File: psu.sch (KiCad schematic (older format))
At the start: 15 parts

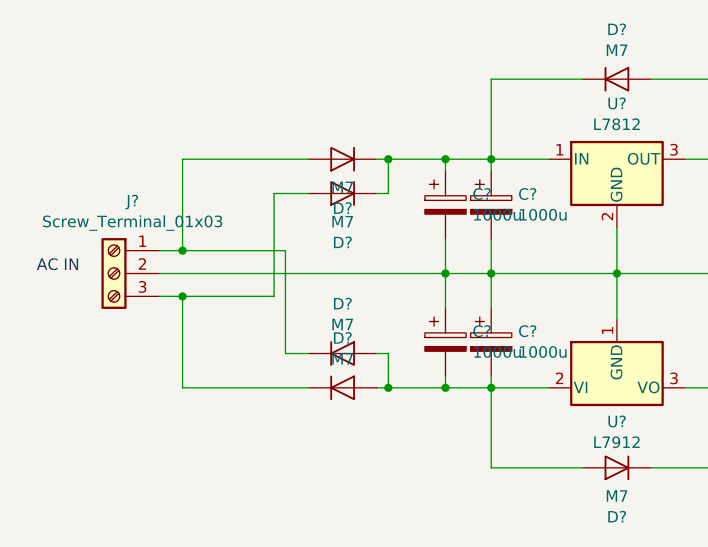
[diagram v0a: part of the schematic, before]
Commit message: adjusted some caps in PSU and rumble filter
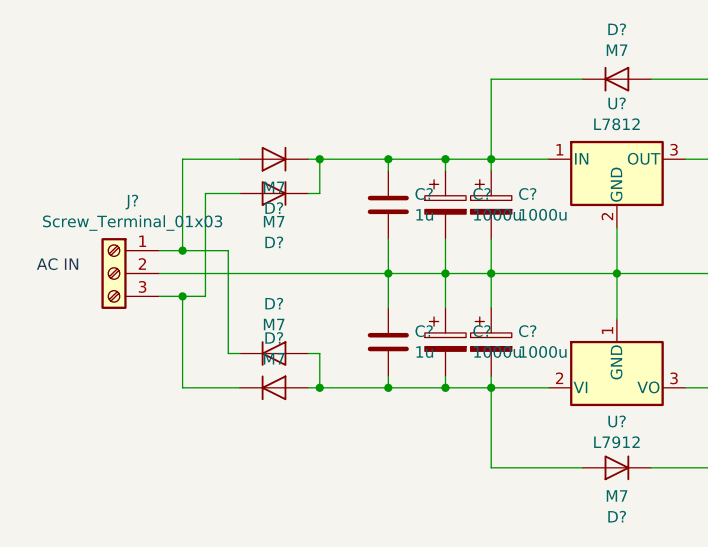
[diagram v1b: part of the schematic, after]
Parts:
- added C? (x2): 1u, Capacitors_SMD:C_0805, symbol Device:C
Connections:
- net GND: now also C?.1, C?.2
- net at C?.1, C?.1, D?.1 (K)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: now also C?.1
- net at C?.2, C?.2, D?.2 (A)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: now also C?.2
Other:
- moved on the sheet: D?
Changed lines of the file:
@@
 	3850 2200 3850 2350
-Wire Wire Line
-	3550 1700 3600 1700
 Wire Wire Line
 	3850 1700 3850 1750
@@
 	4050 1700 4300 1700
 Wire Wire Line
-	3550 2700 3600 2700
+	3250 2700 3300 2700
 Wire Wire Line
 	4050 2650 4050 2700
@@
 L Device:D D?
 U 1 1 61A5C1E5
-P 3400 1700
-F 0 "D?" H 3400 1916 50  0000 C CNN
-F 1 "M7" H 3400 1825 50  0000 C CNN
-F 2 "Diodes_SMD:D_SMA" H 3400 1700 50  0001 C CNN
-F 3 "~" H 3400 1700 50  0001 C CNN
-	1    3400 1700
+P 3100 1700
+F 0 "D?" H 3100 1916 50  0000 C CNN
+F 1 "M7" H 3100 1825 50  0000 C CNN
+F 2 "Diodes_SMD:D_SMA" H 3100 1700 50  0001 C CNN
+F 3 "~" H 3100 1700 50  0001 C CNN
+	1    3100 1700
 	-1   0    0    1
 $EndComp
@@
 L Device:D D?
 U 1 1 61A5C611
-P 3400 1850
-F 0 "D?" H 3400 2066 50  0000 C CNN
-F 1 "M7" H 3400 1975 50  0000 C CNN
-F 2 "Diodes_SMD:D_SMA" H 3400 1850 50  0001 C CNN
-F 3 "~" H 3400 1850 50  0001 C CNN
-	1    3400 1850
+P 3100 1850
+F 0 "D?" H 3100 2066 50  0000 C CNN
+F 1 "M7" H 3100 1975 50  0000 C CNN
+F 2 "Diodes_SMD:D_SMA" H 3100 1850 50  0001 C CNN
+F 3 "~" H 3100 1850 50  0001 C CNN
+	1    3100 1850
 	-1   0    0    1
 $EndComp
@@
 L Device:D D?
 U 1 1 61A5C8F9
-P 3400 2700
-F 0 "D?" H 3400 2916 50  0000 C CNN
-F 1 "M7" H 3400 2825 50  0000 C CNN
-F 2 "Diodes_SMD:D_SMA" H 3400 2700 50  0001 C CNN
-F 3 "~" H 3400 2700 50  0001 C CNN
-	1    3400 2700
+P 3100 2700
+F 0 "D?" H 3100 2916 50  0000 C CNN
+F 1 "M7" H 3100 2825 50  0000 C CNN
+F 2 "Diodes_SMD:D_SMA" H 3100 2700 50  0001 C CNN
+F 3 "~" H 3100 2700 50  0001 C CNN
+	1    3100 2700
 	1    0    0    -1
 $EndComp
@@
 L Device:D D?
 U 1 1 61A5D636
-P 3400 2550
-F 0 "D?" H 3400 2766 50  0000 C CNN
-F 1 "M7" H 3400 2675 50  0000 C CNN
-F 2 "Diodes_SMD:D_SMA" H 3400 2550 50  0001 C CNN
-F 3 "~" H 3400 2550 50  0001 C CNN
-	1    3400 2550
-	1    0    0    -1
-$EndComp
-Wire Wire Line
-	3550 1850 3600 1850
-Wire Wire Line
-	3600 1850 3600 1700
-Wire Wire Line
-	3550 2550 3600 2550
-Wire Wire Line
-	3600 2550 3600 2700
+P 3100 2550
+F 0 "D?" H 3100 2766 50  0000 C CNN
+F 1 "M7" H 3100 2675 50  0000 C CNN
+F 2 "Diodes_SMD:D_SMA" H 3100 2550 50  0001 C CNN
+F 3 "~" H 3100 2550 50  0001 C CNN
+	1    3100 2550
+	1    0    0    -1
+$EndComp
+Wire Wire Line
+	3250 1850 3300 1850
+Wire Wire Line
+	3250 2550 3300 2550
 Wire Wire Line
 	2700 1700 2700 2100
@@
 	2700 2100 2600 2100
 Wire Wire Line
-	2700 1700 3250 1700
-Wire Wire Line
-	2700 2100 3150 2100
-Wire Wire Line
-	3150 2100 3150 2550
-Wire Wire Line
-	3150 2550 3250 2550
+	2600 2300 2700 2300
+Wire Wire Line
+	2700 2300 2700 2700
+Connection ~ 3850 1700
+Connection ~ 3850 2700
+Wire Wire Line
+	2600 2200 3600 2200
+Wire Wire Line
+	3250 1700 3300 1700
+Wire Wire Line
+	3300 1850 3300 1700
+Connection ~ 3300 1700
+Wire Wire Line
+	3300 1700 3600 1700
+Wire Wire Line
+	2700 1700 2950 1700
+Wire Wire Line
+	2700 2700 2950 2700
+Wire Wire Line
+	3300 2550 3300 2700
+Wire Wire Line
+	3300 2700 3600 2700
+Connection ~ 3300 2700
+Wire Wire Line
+	2700 2100 2900 2100
+Wire Wire Line
+	2900 2100 2900 2550
+Wire Wire Line
+	2900 2550 2950 2550
 Connection ~ 2700 2100
 Wire Wire Line
-	2600 2300 2700 2300
-Wire Wire Line
-	2700 2300 2700 2700
-Wire Wire Line
-	2700 2700 3250 2700
-Wire Wire Line
-	2700 2300 3100 2300
-Wire Wire Line
-	3100 2300 3100 1850
-Wire Wire Line
-	3100 1850 3250 1850
+	2800 1850 2800 2300
+Wire Wire Line
+	2800 2300 2700 2300
+Wire Wire Line
+	2800 1850 2950 1850
 Connection ~ 2700 2300
-Wire Wire Line
-	2600 2200 3850 2200
+$Comp
+L Device:C C?
+U 1 1 615DA40F
+P 3600 1900
+F 0 "C?" H 3715 1946 50  0000 L CNN
+F 1 "1u" H 3715 1855 50  0000 L CNN
+F 2 "Capacitors_SMD:C_0805" H 3638 1750 50  0001 C CNN
+F 3 "~" H 3600 1900 50  0001 C CNN
+	1    3600 1900
+	1    0    0    -1
+$EndComp
+$Comp
+L Device:C C?
+U 1 1 615DA6FF
+P 3600 2500
+F 0 "C?" H 3715 2546 50  0000 L CNN
+F 1 "1u" H 3715 2455 50  0000 L CNN
+F 2 "Capacitors_SMD:C_0805" H 3638 2350 50  0001 C CNN
+F 3 "~" H 3600 2500 50  0001 C CNN
+	1    3600 2500
+	1    0    0    -1
+$EndComp
+Wire Wire Line
+	3600 2700 3600 2650
+Connection ~ 3600 2700
+Wire Wire Line
+	3600 2700 3850 2700
+Wire Wire Line
+	3600 2350 3600 2200
+Connection ~ 3600 2200
+Wire Wire Line
+	3600 2200 3850 2200
+Wire Wire Line
+	3600 2200 3600 2050
+Wire Wire Line
+	3600 1750 3600 1700
+Connection ~ 3600 1700
 Wire Wire Line
 	3600 1700 3850 1700
-Connection ~ 3600 1700
-Connection ~ 3850 1700
-Wire Wire Line
-	3600 2700 3850 2700
-Connection ~ 3600 2700
-Connection ~ 3850 2700
 $EndSCHEMATC

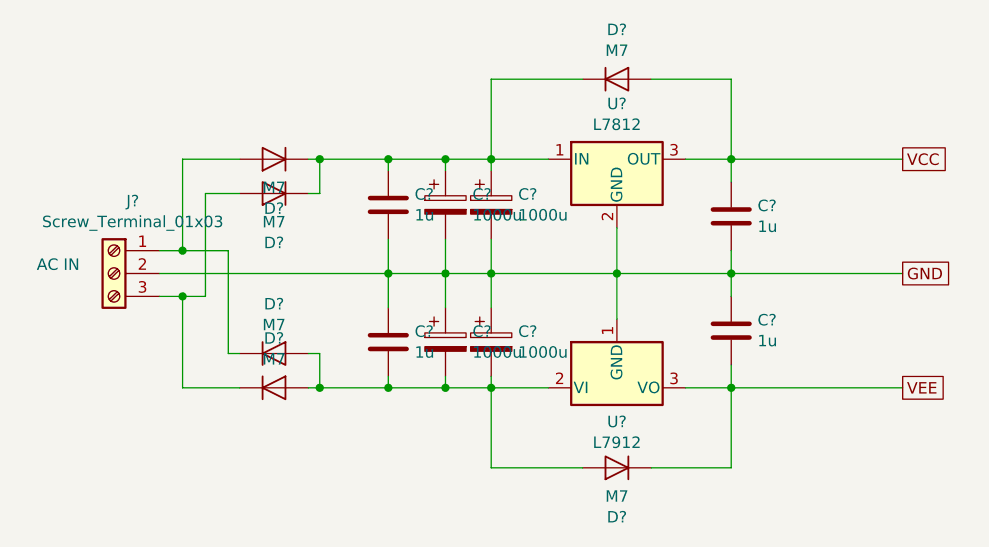
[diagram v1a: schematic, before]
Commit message: improved PSU, gain up front, reordered filter stages, shrunk rumble filter
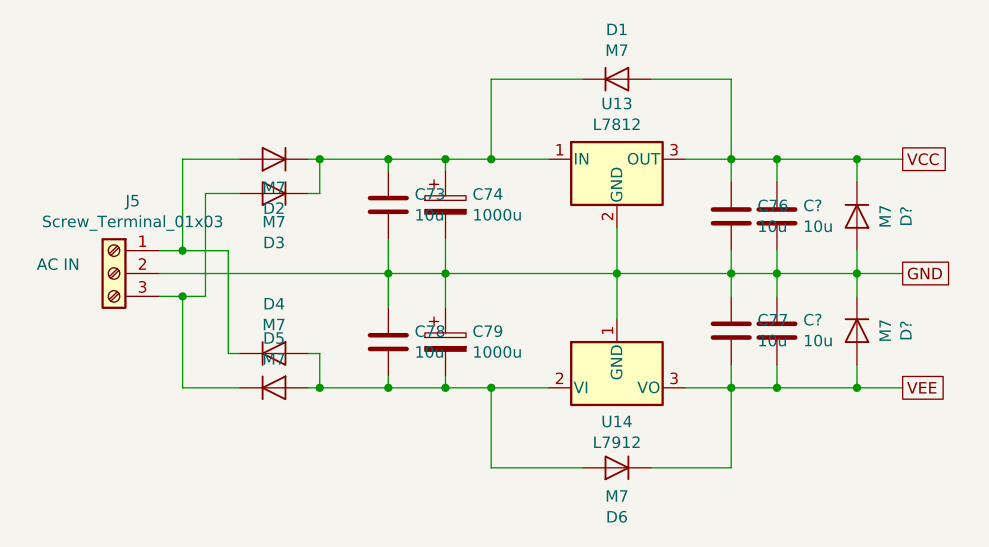
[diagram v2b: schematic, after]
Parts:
- removed C? (x2): 1000u, Capacitors_ThroughHole:CP_Radial_D16.0mm_P7.50mm, symbol Device:CP
- added C? (x2): 10u, Capacitors_SMD:C_0805, symbol Device:C
- added D? (x2): M7, Diodes_SMD:D_SMA, symbol Device:D
- C73, C76, C77, C78: renamed from C?; value 1u -> 10u
- J5: renamed from J?; footprint (none) -> Terminals_Phoenix:TerminalBlock_Phoenix_MKDS1.5-3pol
- gave numbers to parts that had none: 10
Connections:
- net GND: now also C?.1, C?.2, D?.1 (K), D?.2 (A)
- net VCC: now also C?.1, D?.1 (K)
- net VEE: now also C?.2, D?.2 (A)
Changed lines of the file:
@@
 $EndDescr
 $Comp
-L Connector:Screw_Terminal_01x03 J?
+L Connector:Screw_Terminal_01x03 J5
 U 1 1 61A2D78B
 P 2400 2200
-F 0 "J?" H 2318 2517 50  0000 C CNN
+F 0 "J5" H 2318 2517 50  0000 C CNN
 F 1 "Screw_Terminal_01x03" H 2318 2426 50  0000 C CNN
-F 2 "" H 2400 2200 50  0001 C CNN
+F 2 "Terminals_Phoenix:TerminalBlock_Phoenix_MKDS1.5-3pol" H 2400 2200 50  0001 C CNN
 F 3 "~" H 2400 2200 50  0001 C CNN
 	1    2400 2200
@@
 $EndComp
 $Comp
-L Regulator_Linear:L7812 U?
+L Regulator_Linear:L7812 U13
 U 1 1 61A2F137
 P 4600 1700
-F 0 "U?" H 4600 1942 50  0000 C CNN
+F 0 "U13" H 4600 1942 50  0000 C CNN
 F 1 "L7812" H 4600 1851 50  0000 C CNN
 F 2 "Power_Integrations:TO-220" H 4625 1550 50  0001 L CIN
@@
 $EndComp
 $Comp
-L Regulator_Linear:L7912 U?
+L Regulator_Linear:L7912 U14
 U 1 1 61A2F6A1
 P 4600 2700
-F 0 "U?" H 4600 2551 50  0000 C CNN
+F 0 "U14" H 4600 2551 50  0000 C CNN
 F 1 "L7912" H 4600 2460 50  0000 C CNN
 F 2 "Power_Integrations:TO-220" H 4600 2500 50  0001 C CIN
@@
 AC IN
 $Comp
-L Device:CP C?
+L Device:CP C74
 U 1 1 61A39623
 P 3850 1900
-F 0 "C?" H 3968 1946 50  0000 L CNN
+F 0 "C74" H 3968 1946 50  0000 L CNN
 F 1 "1000u" H 3968 1855 50  0000 L CNN
 F 2 "Capacitors_ThroughHole:CP_Radial_D16.0mm_P7.50mm" H 3888 1750 50  0001 C CNN
@@
 $EndComp
 $Comp
-L Device:CP C?
-U 1 1 61A39AC3
-P 4050 1900
-F 0 "C?" H 4168 1946 50  0000 L CNN
-F 1 "1000u" H 4168 1855 50  0000 L CNN
-F 2 "Capacitors_ThroughHole:CP_Radial_D16.0mm_P7.50mm" H 4088 1750 50  0001 C CNN
-F 3 "~" H 4050 1900 50  0001 C CNN
-	1    4050 1900
-	1    0    0    -1
-$EndComp
-$Comp
-L Device:CP C?
+L Device:CP C79
 U 1 1 61A3D77A
 P 3850 2500
-F 0 "C?" H 3968 2546 50  0000 L CNN
+F 0 "C79" H 3968 2546 50  0000 L CNN
 F 1 "1000u" H 3968 2455 50  0000 L CNN
 F 2 "Capacitors_ThroughHole:CP_Radial_D16.0mm_P7.50mm" H 3888 2350 50  0001 C CNN
@@
 Connection ~ 3850 2200
 Wire Wire Line
-	3850 2200 4050 2200
-$Comp
-L Device:CP C?
-U 1 1 61A42A77
-P 4050 2500
-F 0 "C?" H 4168 2546 50  0000 L CNN
-F 1 "1000u" H 4168 2455 50  0000 L CNN
-F 2 "Capacitors_ThroughHole:CP_Radial_D16.0mm_P7.50mm" H 4088 2350 50  0001 C CNN
-F 3 "~" H 4050 2500 50  0001 C CNN
-	1    4050 2500
-	1    0    0    -1
-$EndComp
-Wire Wire Line
-	4050 2050 4050 2200
-Wire Wire Line
-	4050 2200 4050 2350
-Connection ~ 4050 2200
-Wire Wire Line
 	3850 2200 3850 2350
 Wire Wire Line
@@
 Wire Wire Line
 	3850 1700 4050 1700
-Wire Wire Line
-	4050 1700 4050 1750
 Connection ~ 4050 1700
 Wire Wire Line
@@
 Wire Wire Line
 	3250 2700 3300 2700
-Wire Wire Line
-	4050 2650 4050 2700
 Connection ~ 4050 2700
 Wire Wire Line
@@
 Wire Wire Line
 	3850 2700 4050 2700
-Wire Wire Line
-	4050 2200 4600 2200
 Wire Wire Line
 	4600 2200 4600 2000
@@
 	4900 2700 5100 2700
 $Comp
-L Device:C C?
+L Device:C C76
 U 1 1 61A4AEE8
 P 5100 1950
-F 0 "C?" H 5215 1996 50  0000 L CNN
-F 1 "1u" H 5215 1905 50  0000 L CNN
+F 0 "C76" H 5215 1996 50  0000 L CNN
+F 1 "10u" H 5215 1905 50  0000 L CNN
 F 2 "Capacitors_SMD:C_0805" H 5138 1800 50  0001 C CNN
 F 3 "~" H 5100 1950 50  0001 C CNN
@@
 Connection ~ 5100 1700
 Wire Wire Line
-	5100 1700 5850 1700
+	5100 1700 5300 1700
 Wire Wire Line
 	5100 2100 5100 2200
 Connection ~ 5100 2200
 Wire Wire Line
-	5100 2200 5850 2200
-$Comp
-L Device:C C?
+	5100 2200 5300 2200
+$Comp
+L Device:C C77
 U 1 1 61A4C047
 P 5100 2450
-F 0 "C?" H 5215 2496 50  0000 L CNN
-F 1 "1u" H 5215 2405 50  0000 L CNN
+F 0 "C77" H 5215 2496 50  0000 L CNN
+F 1 "10u" H 5215 2405 50  0000 L CNN
 F 2 "Capacitors_SMD:C_0805" H 5138 2300 50  0001 C CNN
 F 3 "~" H 5100 2450 50  0001 C CNN
@@
 Connection ~ 5100 2700
 Wire Wire Line
-	5100 2700 5850 2700
-$Comp
-L Device:D D?
+	5100 2700 5300 2700
+$Comp
+L Device:D D1
 U 1 1 61A4D531
 P 4600 1350
-F 0 "D?" H 4600 1566 50  0000 C CNN
+F 0 "D1" H 4600 1566 50  0000 C CNN
 F 1 "M7" H 4600 1475 50  0000 C CNN
 F 2 "Diodes_SMD:D_SMA" H 4600 1350 50  0001 C CNN
@@
 $EndComp
 $Comp
-L Device:D D?
+L Device:D D6
 U 1 1 61A561AB
 P 4600 3050
-F 0 "D?" H 4600 3266 50  0000 C CNN
+F 0 "D6" H 4600 3266 50  0000 C CNN
 F 1 "M7" H 4600 3175 50  0000 C CNN
 F 2 "Diodes_SMD:D_SMA" H 4600 3050 50  0001 C CNN
@@
 	4750 3050 5100 3050
 $Comp
-L Device:D D?
+L Device:D D2
 U 1 1 61A5C1E5
 P 3100 1700
-F 0 "D?" H 3100 1916 50  0000 C CNN
+F 0 "D2" H 3100 1916 50  0000 C CNN
 F 1 "M7" H 3100 1825 50  0000 C CNN
 F 2 "Diodes_SMD:D_SMA" H 3100 1700 50  0001 C CNN
@@
 $EndComp
 $Comp
-L Device:D D?
+L Device:D D3
 U 1 1 61A5C611
 P 3100 1850
-F 0 "D?" H 3100 2066 50  0000 C CNN
+F 0 "D3" H 3100 2066 50  0000 C CNN
 F 1 "M7" H 3100 1975 50  0000 C CNN
 F 2 "Diodes_SMD:D_SMA" H 3100 1850 50  0001 C CNN
@@
 $EndComp
 $Comp
-L Device:D D?
+L Device:D D5
 U 1 1 61A5C8F9
 P 3100 2700
-F 0 "D?" H 3100 2916 50  0000 C CNN
+F 0 "D5" H 3100 2916 50  0000 C CNN
 F 1 "M7" H 3100 2825 50  0000 C CNN
 F 2 "Diodes_SMD:D_SMA" H 3100 2700 50  0001 C CNN
@@
 $EndComp
 $Comp
-L Device:D D?
+L Device:D D4
 U 1 1 61A5D636
 P 3100 2550
-F 0 "D?" H 3100 2766 50  0000 C CNN
+F 0 "D4" H 3100 2766 50  0000 C CNN
 F 1 "M7" H 3100 2675 50  0000 C CNN
 F 2 "Diodes_SMD:D_SMA" H 3100 2550 50  0001 C CNN
@@
 Connection ~ 2700 2300
 $Comp
-L Device:C C?
+L Device:C C73
 U 1 1 615DA40F
 P 3600 1900
-F 0 "C?" H 3715 1946 50  0000 L CNN
-F 1 "1u" H 3715 1855 50  0000 L CNN
+F 0 "C73" H 3715 1946 50  0000 L CNN
+F 1 "10u" H 3715 1855 50  0000 L CNN
 F 2 "Capacitors_SMD:C_0805" H 3638 1750 50  0001 C CNN
 F 3 "~" H 3600 1900 50  0001 C CNN
@@
 $EndComp
 $Comp
-L Device:C C?
+L Device:C C78
 U 1 1 615DA6FF
 P 3600 2500
-F 0 "C?" H 3715 2546 50  0000 L CNN
-F 1 "1u" H 3715 2455 50  0000 L CNN
+F 0 "C78" H 3715 2546 50  0000 L CNN
+F 1 "10u" H 3715 2455 50  0000 L CNN
 F 2 "Capacitors_SMD:C_0805" H 3638 2350 50  0001 C CNN
 F 3 "~" H 3600 2500 50  0001 C CNN
@@
 Wire Wire Line
 	3600 1700 3850 1700
+$Comp
+L Device:C C?
+U 1 1 615FF89D
+P 5300 1950
+F 0 "C?" H 5415 1996 50  0000 L CNN
+F 1 "10u" H 5415 1905 50  0000 L CNN
+F 2 "Capacitors_SMD:C_0805" H 5338 1800 50  0001 C CNN
+F 3 "~" H 5300 1950 50  0001 C CNN
+	1    5300 1950
+	1    0    0    -1
+$EndComp
+$Comp
+L Device:C C?
+U 1 1 615FFB71
+P 5300 2450
+F 0 "C?" H 5415 2496 50  0000 L CNN
+F 1 "10u" H 5415 2405 50  0000 L CNN
+F 2 "Capacitors_SMD:C_0805" H 5338 2300 50  0001 C CNN
+F 3 "~" H 5300 2450 50  0001 C CNN
+	1    5300 2450
+	1    0    0    -1
+$EndComp
+Wire Wire Line
+	5300 1700 5300 1800
+Connection ~ 5300 1700
+Wire Wire Line
+	5300 1700 5650 1700
+Wire Wire Line
+	5300 2100 5300 2200
+Connection ~ 5300 2200
+Wire Wire Line
+	5300 2200 5650 2200
+Wire Wire Line
+	5300 2200 5300 2300
+Connection ~ 5300 2700
+Wire Wire Line
+	5300 2700 5650 2700
+Wire Wire Line
+	5300 2600 5300 2700
+Wire Wire Line
+	3850 2200 4600 2200
+$Comp
+L Device:D D?
+U 1 1 61608971
+P 5650 1950
+F 0 "D?" H 5650 2166 50  0000 C CNN
+F 1 "M7" H 5650 2075 50  0000 C CNN
+F 2 "Diodes_SMD:D_SMA" H 5650 1950 50  0001 C CNN
+F 3 "~" H 5650 1950 50  0001 C CNN
+	1    5650 1950
+	0    1    1    0
+$EndComp
+$Comp
+L Device:D D?
+U 1 1 6160A269
+P 5650 2450
+F 0 "D?" H 5650 2666 50  0000 C CNN
+F 1 "M7" H 5650 2575 50  0000 C CNN
+F 2 "Diodes_SMD:D_SMA" H 5650 2450 50  0001 C CNN
+F 3 "~" H 5650 2450 50  0001 C CNN
+	1    5650 2450
+	0    1    1    0
+$EndComp
+Wire Wire Line
+	5650 1700 5650 1800
+Connection ~ 5650 1700
+Wire Wire Line
+	5650 1700 5850 1700
+Wire Wire Line
+	5650 2100 5650 2200
+Connection ~ 5650 2200
+Wire Wire Line
+	5650 2200 5850 2200
+Wire Wire Line
+	5650 2200 5650 2300
+Wire Wire Line
+	5650 2600 5650 2700
+Connection ~ 5650 2700
+Wire Wire Line
+	5650 2700 5850 2700
 $EndSCHEMATC
